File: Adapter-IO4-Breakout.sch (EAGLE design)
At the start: 7 parts

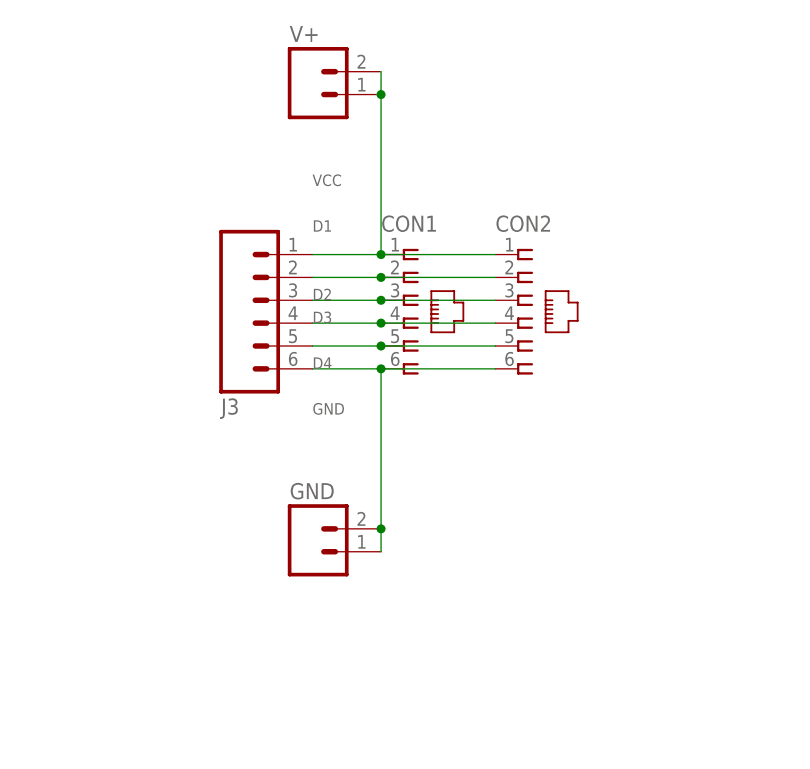
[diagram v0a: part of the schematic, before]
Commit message: added values for connectors
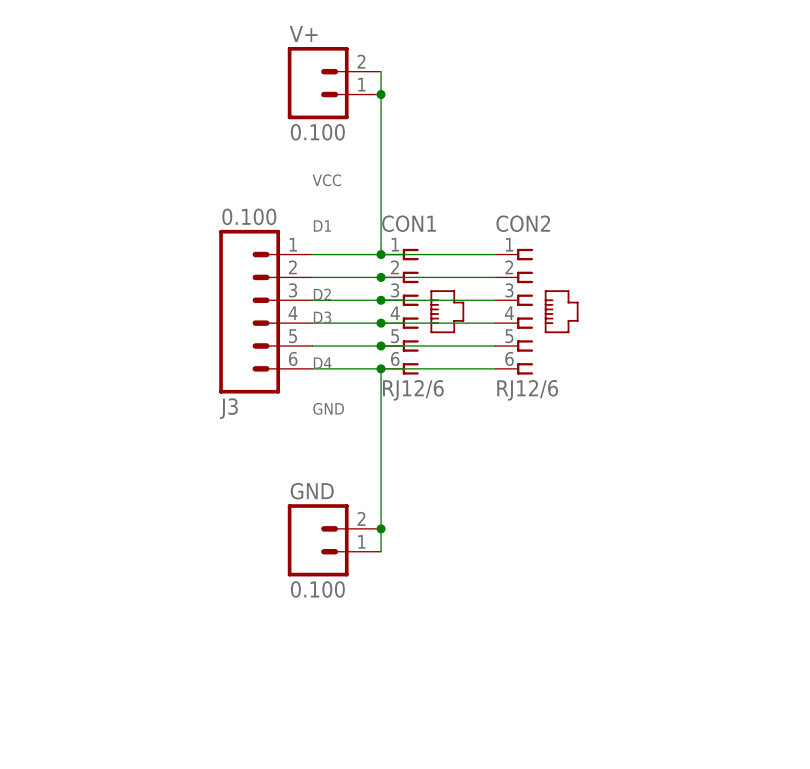
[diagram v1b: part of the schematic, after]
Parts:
- CON1, CON2: value (none) -> RJ12/6
- GND, J3, V+: value (none) -> 0.100
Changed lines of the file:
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@@
 <part name="FRAME1" library="SparkFun" deviceset="FRAME-LETTER" device=""/>
 <part name="U$1" library="SparkFun" deviceset="OSHW-LOGO" device="M"/>
-<part name="J3" library="SPCoast" deviceset="CONNECTOR-M06" device="LOCK"/>
+<part name="J3" library="SPCoast" deviceset="CONNECTOR-M06" device="LOCK" value="0.100"/>
 <part name="BOARD1" library="SPCoast" deviceset="BOARD" device="50X50-HOHOLES"/>
-<part name="V+" library="SPCoast" deviceset="CONNECTOR-M02" device="1X02-LOCK"/>
-<part name="GND" library="SPCoast" deviceset="CONNECTOR-M02" device="1X02-LOCK"/>
-<part name="CON1" library="SPCoast" deviceset="CONNECTOR-RJ25" device="-6P6C"/>
-<part name="CON2" library="SPCoast" deviceset="CONNECTOR-RJ25" device="-6P6C"/>
+<part name="V+" library="SPCoast" deviceset="CONNECTOR-M02" device="1X02-LOCK" value="0.100"/>
+<part name="GND" library="SPCoast" deviceset="CONNECTOR-M02" device="1X02-LOCK" value="0.100"/>
+<part name="CON1" library="SPCoast" deviceset="CONNECTOR-RJ25" device="-6P6C" value="RJ12/6"/>
+<part name="CON2" library="SPCoast" deviceset="CONNECTOR-RJ25" device="-6P6C" value="RJ12/6"/>
 </parts>
 <sheets>

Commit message: normalized values
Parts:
- BOARD1: value BOARD50X50-HOHOLES -> BOARD; device SPCoast:BOARD50X50-HOHOLES -> SPCoast:BOARD50X50-NOHOLES
- U$1: value OSHW-LOGOM -> OSHW
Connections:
- net GND: now also GND.A, GND.B; no longer GND.1, GND.2
- net VCC: now also V+.A, V+.B; no longer V+.1, V+.2
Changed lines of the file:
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@@
 <parts>
 <part name="FRAME1" library="SparkFun" deviceset="FRAME-LETTER" device=""/>
-<part name="U$1" library="SparkFun" deviceset="OSHW-LOGO" device="M"/>
+<part name="U$1" library="SparkFun" deviceset="OSHW-LOGO" device="M" value="OSHW"/>
 <part name="J3" library="SPCoast" deviceset="CONNECTOR-M06" device="LOCK" value="0.100"/>
-<part name="BOARD1" library="SPCoast" deviceset="BOARD" device="50X50-HOHOLES"/>
+<part name="BOARD1" library="SPCoast" deviceset="BOARD" device="50X50-NOHOLES" value="BOARD"/>
 <part name="V+" library="SPCoast" deviceset="CONNECTOR-M02" device="1X02-LOCK" value="0.100"/>
 <part name="GND" library="SPCoast" deviceset="CONNECTOR-M02" device="1X02-LOCK" value="0.100"/>
@@
 <instance part="U$1" gate="G$1" x="17.78" y="12.7"/>
 <instance part="J3" gate="J" x="116.84" y="96.52" rot="MR180"/>
-<instance part="BOARD1" gate="G$1" x="241.3" y="40.64"/>
-<instance part="V+" gate="G$1" x="124.46" y="119.38"/>
-<instance part="GND" gate="G$1" x="124.46" y="68.58"/>
+<instance part="BOARD1" gate="B" x="241.3" y="40.64"/>
+<instance part="V+" gate="J" x="124.46" y="119.38"/>
+<instance part="GND" gate="J" x="124.46" y="68.58"/>
 <instance part="CON1" gate="J" x="132.08" y="96.52"/>
 <instance part="CON2" gate="J" x="144.78" y="96.52"/>
@@
 <wire x1="129.54" y1="101.6" x2="142.24" y2="101.6" width="0.1524" layer="91"/>
 <pinref part="J3" gate="J" pin="1"/>
-<pinref part="V+" gate="G$1" pin="2"/>
-<pinref part="V+" gate="G$1" pin="1"/>
+<pinref part="V+" gate="J" pin="B"/>
+<pinref part="V+" gate="J" pin="A"/>
 <wire x1="129.54" y1="121.92" x2="129.54" y2="119.38" width="0.1524" layer="91"/>
 <wire x1="129.54" y1="119.38" x2="129.54" y2="101.6" width="0.1524" layer="91"/>
@@
 <wire x1="129.54" y1="88.9" x2="142.24" y2="88.9" width="0.1524" layer="91"/>
 <pinref part="J3" gate="J" pin="6"/>
-<pinref part="GND" gate="G$1" pin="2"/>
+<pinref part="GND" gate="J" pin="B"/>
 <wire x1="129.54" y1="88.9" x2="129.54" y2="71.12" width="0.1524" layer="91"/>
-<pinref part="GND" gate="G$1" pin="1"/>
+<pinref part="GND" gate="J" pin="A"/>
 <wire x1="129.54" y1="71.12" x2="129.54" y2="68.58" width="0.1524" layer="91"/>
 <junction x="129.54" y="71.12"/>
